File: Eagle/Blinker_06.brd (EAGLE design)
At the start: 91.4 x 68.2 mm, 51 parts

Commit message: Net Width
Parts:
- removed U$5: TP_10", SUPPLY:TP_10
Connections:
- net GND: no longer U$5.P$1
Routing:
- net BLAULICHT: track 58.0 -> 52.0 mm
- net N$21: track 56.0 -> 51.5 mm
- net N$16: track 38.4 -> 34.7 mm
- net N$19: track 36.4 -> 34.2 mm
- net N$15: track 27.0 -> 26.2 mm
- net GND: vias 0 -> 1
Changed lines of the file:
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@@
 <setting verticaltext="up"/>
 </settings>
-<grid distance="0.003333" unitdist="inch" unit="inch" style="lines" multiple="1" display="yes" altdistance="25" altunitdist="mil" altunit="mil"/>
+<grid distance="0.05" unitdist="inch" unit="mil" style="lines" multiple="1" display="yes" altdistance="0.025" altunitdist="inch" altunit="inch"/>
 <layers>
 <layer number="1" name="Top" color="4" fill="1" visible="yes" active="yes"/>
@@
 <element name="S2" library="switch" package="TL3XPO" value="TL32PO" x="2.54" y="-7.62" rot="R90"/>
 <element name="U$1" library="SUPPLY" package="TP_10" value="TP_10&quot;" x="71.12" y="35.56"/>
-<element name="U$5" library="SUPPLY" package="TP_10" value="TP_10&quot;" x="63.5" y="38.1"/>
 </elements>
 <signals>
@@
 <wire x1="12.7" y1="33.02" x2="24.13" y2="33.02" width="1.27" layer="16"/>
 <wire x1="24.13" y1="33.02" x2="27.94" y2="36.83" width="1.27" layer="16"/>
-<wire x1="34.29" y1="33.02" x2="45.72" y2="33.02" width="1.27" layer="16"/>
-<wire x1="45.72" y1="33.02" x2="49.53" y2="36.83" width="1.27" layer="16"/>
 <wire x1="71.12" y1="33.02" x2="68.58" y2="33.02" width="1.27" layer="16"/>
 <wire x1="68.58" y1="33.02" x2="67.31" y2="34.29" width="1.27" layer="16"/>
@@
 <wire x1="73.66" y1="50.8" x2="74.93" y2="52.07" width="1.27" layer="16"/>
 <wire x1="74.93" y1="52.07" x2="80.01" y2="52.07" width="1.27" layer="16"/>
-<contactref element="U$5" pad="P$1"/>
-<wire x1="55.88" y1="38.1" x2="63.5" y2="38.1" width="1.27" layer="1"/>
-<wire x1="63.5" y1="38.1" x2="67.31" y2="38.1" width="1.27" layer="16"/>
+<wire x1="67.31" y1="38.1" x2="63.5" y2="38.1" width="1.27" layer="16"/>
+<wire x1="63.5" y1="38.1" x2="55.88" y2="38.1" width="1.27" layer="1"/>
+<via x="63.5" y="38.1" extent="1-16" drill="0.6"/>
+<wire x1="34.29" y1="33.02" x2="45.72" y2="33.02" width="1.27" layer="16"/>
+<wire x1="45.72" y1="33.02" x2="49.53" y2="36.83" width="1.27" layer="16"/>
 </signal>
 <signal name="+12V">
@@
 <contactref element="LED_DRIVER_2" pad="-VOUT@1"/>
 <wire x1="49.53" y1="64.77" x2="49.53" y2="62.23" width="0.4064" layer="16"/>
-<wire x1="49.53" y1="62.23" x2="49.53" y2="59.69" width="0.4064" layer="1"/>
-<wire x1="49.53" y1="59.69" x2="48.26" y2="58.42" width="0.4064" layer="1"/>
-<wire x1="48.26" y1="58.42" x2="16.51" y2="58.42" width="0.4064" layer="1"/>
-<wire x1="16.51" y1="58.42" x2="15.24" y2="57.15" width="0.4064" layer="1"/>
-<wire x1="6.35" y1="46.99" x2="6.35" y2="48.26" width="0.4064" layer="1"/>
-<wire x1="6.35" y1="48.26" x2="7.62" y2="49.53" width="0.4064" layer="1"/>
-<wire x1="7.62" y1="49.53" x2="13.97" y2="49.53" width="0.4064" layer="1"/>
-<wire x1="13.97" y1="49.53" x2="15.24" y2="50.8" width="0.4064" layer="1"/>
-<wire x1="15.24" y1="50.8" x2="15.24" y2="57.15" width="0.4064" layer="1"/>
+<wire x1="6.35" y1="46.99" x2="11.43" y2="52.07" width="0.8128" layer="1"/>
+<wire x1="11.43" y1="52.07" x2="39.37" y2="52.07" width="0.8128" layer="1"/>
+<wire x1="39.37" y1="52.07" x2="49.53" y2="62.23" width="0.8128" layer="1"/>
 </signal>
 <signal name="N$10">
@@
 <contactref element="PLUG-12" pad="1"/>
 <wire x1="12.7" y1="64.77" x2="12.7" y2="62.23" width="0.4064" layer="16"/>
-<wire x1="6.35" y1="62.23" x2="12.7" y2="62.23" width="0.4064" layer="1"/>
+<wire x1="6.35" y1="62.23" x2="12.7" y2="62.23" width="0.8128" layer="1"/>
 </signal>
 <signal name="N$15">
@@
 <contactref element="PLUG-12" pad="2"/>
 <wire x1="27.94" y1="64.77" x2="27.94" y2="62.23" width="0.4064" layer="16"/>
-<wire x1="6.35" y1="57.15" x2="11.43" y2="57.15" width="0.4064" layer="1"/>
-<wire x1="11.43" y1="57.15" x2="12.7" y2="58.42" width="0.4064" layer="1"/>
-<wire x1="12.7" y1="58.42" x2="12.7" y2="59.69" width="0.4064" layer="1"/>
-<wire x1="12.7" y1="59.69" x2="13.97" y2="60.96" width="0.4064" layer="1"/>
-<wire x1="13.97" y1="60.96" x2="26.67" y2="60.96" width="0.4064" layer="1"/>
-<wire x1="26.67" y1="60.96" x2="27.94" y2="62.23" width="0.4064" layer="1"/>
+<wire x1="27.94" y1="62.23" x2="22.86" y2="57.15" width="0.8128" layer="1"/>
+<wire x1="22.86" y1="57.15" x2="6.35" y2="57.15" width="0.8128" layer="1"/>
 </signal>
 <signal name="N$16">
@@
 <contactref element="PLUG-12" pad="3"/>
 <wire x1="34.29" y1="64.77" x2="34.29" y2="62.23" width="0.4064" layer="16"/>
-<wire x1="34.29" y1="62.23" x2="34.29" y2="60.96" width="0.4064" layer="1"/>
-<wire x1="34.29" y1="60.96" x2="33.02" y2="59.69" width="0.4064" layer="1"/>
-<wire x1="33.02" y1="59.69" x2="15.24" y2="59.69" width="0.4064" layer="1"/>
-<wire x1="15.24" y1="59.69" x2="13.97" y2="58.42" width="0.4064" layer="1"/>
-<wire x1="13.97" y1="58.42" x2="13.97" y2="53.34" width="0.4064" layer="1"/>
-<wire x1="13.97" y1="53.34" x2="12.7" y2="52.07" width="0.4064" layer="1"/>
-<wire x1="12.7" y1="52.07" x2="6.35" y2="52.07" width="0.4064" layer="1"/>
+<wire x1="6.35" y1="52.07" x2="8.89" y2="54.61" width="0.8128" layer="1"/>
+<wire x1="8.89" y1="54.61" x2="26.67" y2="54.61" width="0.8128" layer="1"/>
+<wire x1="26.67" y1="54.61" x2="34.29" y2="62.23" width="0.8128" layer="1"/>
 </signal>
 <signal name="N$17">
@@
 <contactref element="PLUG-12" pad="12"/>
 <wire x1="12.7" y1="7.62" x2="12.7" y2="5.08" width="0.4064" layer="16"/>
-<wire x1="6.35" y1="6.35" x2="8.89" y2="6.35" width="0.4064" layer="1"/>
-<wire x1="8.89" y1="6.35" x2="10.16" y2="7.62" width="0.4064" layer="1"/>
-<wire x1="10.16" y1="7.62" x2="12.7" y2="7.62" width="0.4064" layer="1"/>
+<wire x1="12.7" y1="7.62" x2="10.16" y2="7.62" width="0.8128" layer="1"/>
+<wire x1="10.16" y1="7.62" x2="8.89" y2="6.35" width="0.8128" layer="1"/>
+<wire x1="8.89" y1="6.35" x2="6.35" y2="6.35" width="0.8128" layer="1"/>
 </signal>
 <signal name="N$18">
@@
 <contactref element="PLUG-12" pad="11"/>
 <wire x1="27.94" y1="7.62" x2="27.94" y2="5.08" width="0.4064" layer="16"/>
-<wire x1="27.94" y1="7.62" x2="26.67" y2="8.89" width="0.4064" layer="1"/>
-<wire x1="6.35" y1="11.43" x2="12.7" y2="11.43" width="0.4064" layer="1"/>
-<wire x1="26.67" y1="8.89" x2="15.24" y2="8.89" width="0.4064" layer="1"/>
-<wire x1="15.24" y1="8.89" x2="12.7" y2="11.43" width="0.4064" layer="1"/>
+<wire x1="27.94" y1="7.62" x2="24.13" y2="11.43" width="0.8128" layer="1"/>
+<wire x1="24.13" y1="11.43" x2="6.35" y2="11.43" width="0.8128" layer="1"/>
 </signal>
 <signal name="N$19">
@@
 <contactref element="PLUG-12" pad="10"/>
 <wire x1="34.29" y1="7.62" x2="34.29" y2="5.08" width="0.4064" layer="16"/>
-<wire x1="34.29" y1="7.62" x2="34.29" y2="8.89" width="0.4064" layer="1"/>
-<wire x1="34.29" y1="8.89" x2="33.02" y2="10.16" width="0.4064" layer="1"/>
-<wire x1="33.02" y1="10.16" x2="16.51" y2="10.16" width="0.4064" layer="1"/>
-<wire x1="16.51" y1="10.16" x2="13.97" y2="12.7" width="0.4064" layer="1"/>
-<wire x1="13.97" y1="12.7" x2="13.97" y2="15.24" width="0.4064" layer="1"/>
-<wire x1="13.97" y1="15.24" x2="12.7" y2="16.51" width="0.4064" layer="1"/>
-<wire x1="12.7" y1="16.51" x2="6.35" y2="16.51" width="0.4064" layer="1"/>
+<wire x1="34.29" y1="7.62" x2="25.4" y2="16.51" width="0.8128" layer="1"/>
+<wire x1="25.4" y1="16.51" x2="6.35" y2="16.51" width="0.8128" layer="1"/>
 </signal>
 <signal name="N$21">
@@
 <contactref element="PLUG-12" pad="9"/>
 <wire x1="49.53" y1="7.62" x2="49.53" y2="5.08" width="0.4064" layer="16"/>
-<wire x1="49.53" y1="7.62" x2="49.53" y2="10.16" width="0.4064" layer="1"/>
-<wire x1="49.53" y1="10.16" x2="48.26" y2="11.43" width="0.4064" layer="1"/>
-<wire x1="48.26" y1="11.43" x2="17.78" y2="11.43" width="0.4064" layer="1"/>
-<wire x1="17.78" y1="11.43" x2="15.24" y2="13.97" width="0.4064" layer="1"/>
-<wire x1="6.35" y1="21.59" x2="6.35" y2="20.32" width="0.4064" layer="1"/>
-<wire x1="6.35" y1="20.32" x2="7.62" y2="19.05" width="0.4064" layer="1"/>
-<wire x1="7.62" y1="19.05" x2="13.97" y2="19.05" width="0.4064" layer="1"/>
-<wire x1="13.97" y1="19.05" x2="15.24" y2="17.78" width="0.4064" layer="1"/>
-<wire x1="15.24" y1="17.78" x2="15.24" y2="13.97" width="0.4064" layer="1"/>
+<wire x1="49.53" y1="7.62" x2="35.56" y2="21.59" width="0.8128" layer="1"/>
+<wire x1="35.56" y1="21.59" x2="6.35" y2="21.59" width="0.8128" layer="1"/>
 </signal>
 <signal name="INDICATOR-LEFT">
@@
 <wire x1="68.58" y1="43.18" x2="67.31" y2="44.45" width="0.4064" layer="1"/>
 <wire x1="67.31" y1="44.45" x2="58.42" y2="44.45" width="0.4064" layer="1"/>
-<wire x1="6.35" y1="43.18" x2="6.35" y2="41.91" width="0" layer="19" extent="1-16"/>
 <wire x1="58.42" y1="44.45" x2="55.88" y2="46.99" width="0.4064" layer="1"/>
 <wire x1="55.88" y1="46.99" x2="10.16" y2="46.99" width="0.4064" layer="1"/>

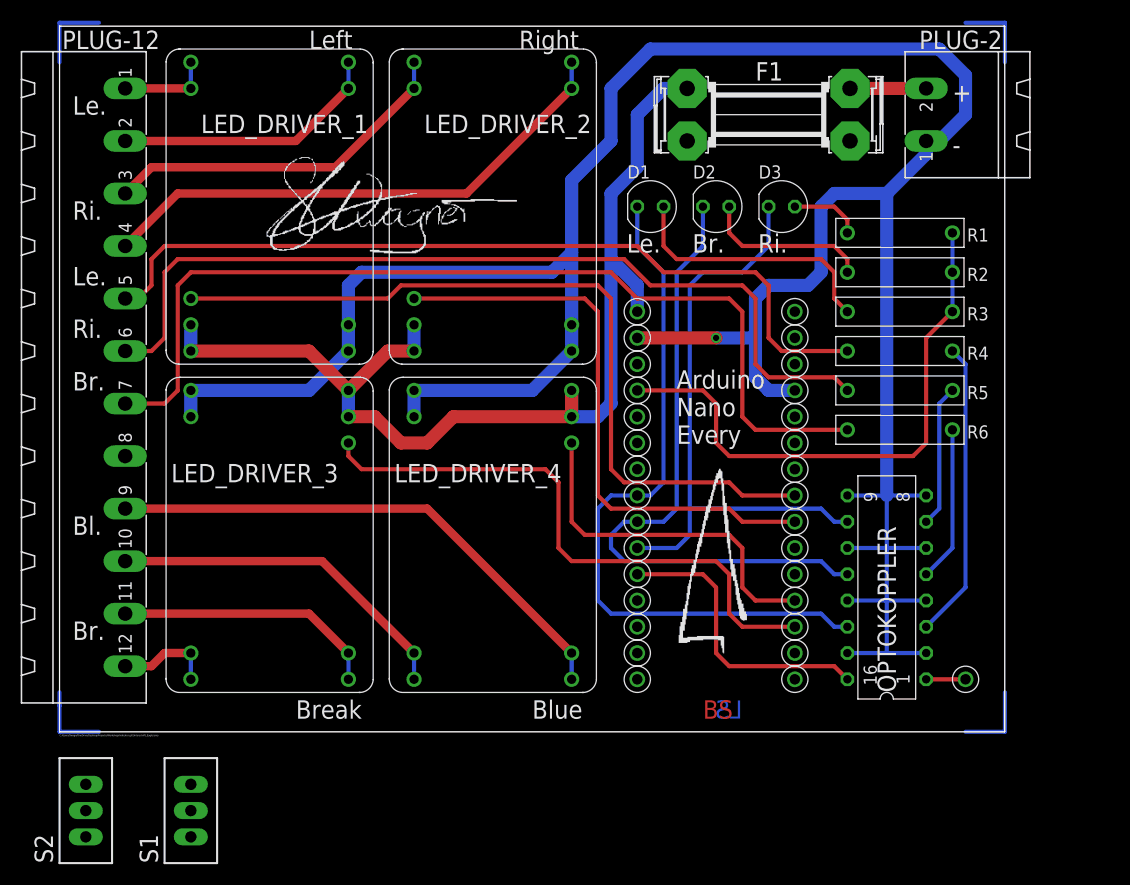
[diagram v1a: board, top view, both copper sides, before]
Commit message: GY-61 introduction
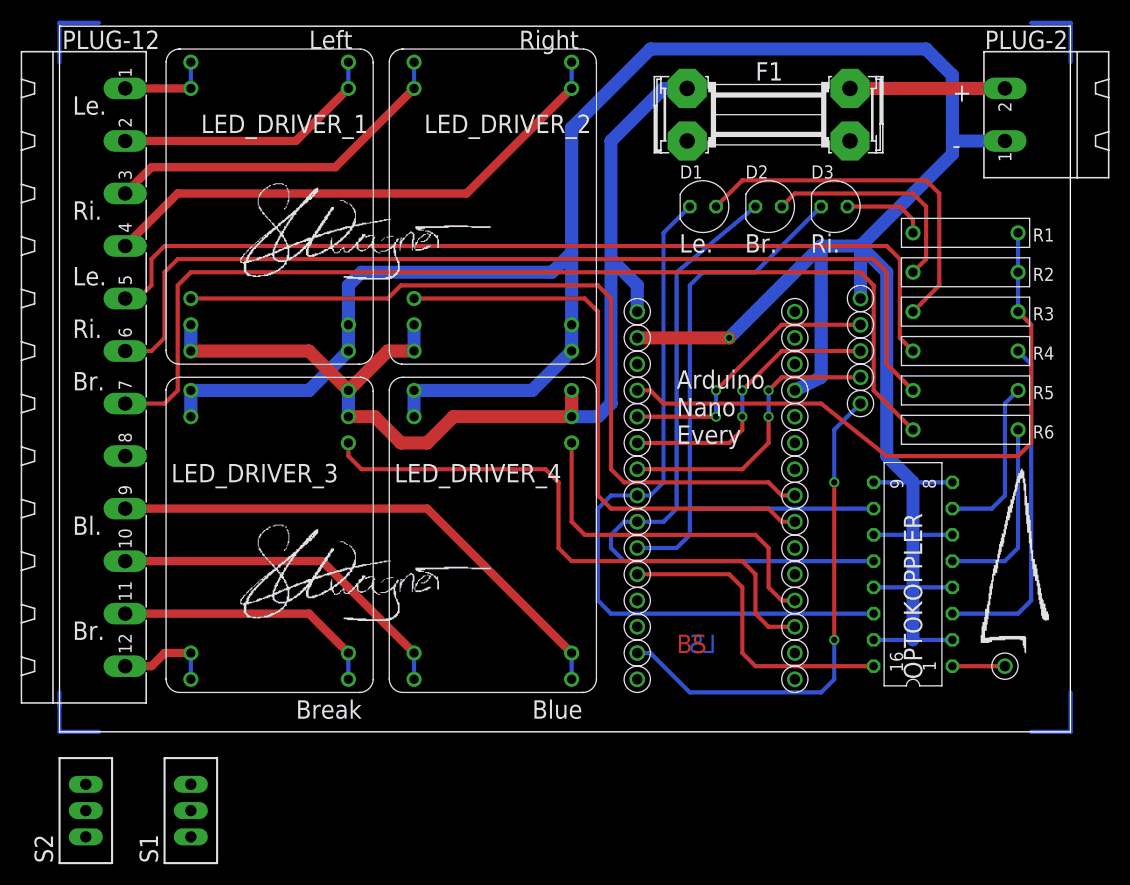
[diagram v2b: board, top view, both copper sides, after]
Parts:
- added GND_GY-61, VCC-GY-61, X_OUT, Y_OUT, Z_OUT: TP_10", SUPPLY:TP_10
- moved U$1 31.8 mm to (55.9, 7.62)
- moved U$42 27.9 mm to (55.9, 35.6)
- moved U$45 27.5 mm to (71.1, 35.6)
- moved U$50 22.9 mm to (55.9, 12.7)
- moved U$44 18.3 mm to (71.1, 17.8)
- moved U$56 17.0 mm to (55.9, 25.4)
- moved U$43 15.5 mm to (71.1, 27.9)
- moved U$49 15.2 mm to (55.9, 27.9)
- moved PLUG-2 7.62 mm to (96.5, 59.7)
- moved R1 6.35 mm to (87.6, 48.3)
- moved R2 6.35 mm to (87.6, 44.5)
- moved R3 6.35 mm to (87.6, 40.6)
- moved R4 6.35 mm to (87.6, 36.8)
- moved R5 6.35 mm to (87.6, 33.0)
- moved R6 6.35 mm to (87.6, 29.2)
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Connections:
- new net N$12: U$56.P$1, X_OUT.P$1
- new net N$13: U$49.P$1, Y_OUT.P$1
- new net N$23: U$48.P$1, Z_OUT.P$1
- new net N$9: U$1.P$1, VCC-GY-61.P$1
- net GND: now also GND_GY-61.P$1
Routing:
- net N$9: track 0.00 -> 48.9 mm, vias 0 -> 2
- net N$12: track 0.00 -> 28.2 mm, vias 0 -> 2
- net N$13: track 0.00 -> 27.5 mm, vias 0 -> 2
- net N$23: track 0.00 -> 26.8 mm, vias 0 -> 2
- net GND: track 266.1 -> 287.7 mm
- net LED_2: track 25.7 -> 35.7 mm
- net INDICATOR-RIGHT: track 86.2 -> 94.1 mm
- net INDICATOR-LEFT: track 80.6 -> 88.5 mm
- net N$1: track 7.37 -> 15.0 mm
- net +5V: track 54.7 -> 61.8 mm
- net BREAK: track 93.3 -> 99.7 mm
- net N$20: track 16.3 -> 21.9 mm
- net SCH_LI_3: track 58.5 -> 63.4 mm
- net N$4: track 62.8 -> 67.4 mm
- net N$24: track 28.8 -> 32.8 mm
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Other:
- board size 91.4 x 68.2 mm -> 97.8 x 68.2 mm
- board text removed: "C:/Users/Swagn/OneDrive/Desktop/Projecte/Workshop/Indicator.git/Unterschrift_Eagle.bmp"
